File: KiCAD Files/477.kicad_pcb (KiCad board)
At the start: 2 copper layers, 101.7 x 59.5 mm, 74 parts, among them IC1 W25N01GVSFIG, IC2 W25N01GVSFIG, IC3 W25N01GVSFIG, IC4 W25N01GVSFIG, IC5 AZ1117IH-3.3TRG1, IC6 USBLC6-2SC6, J1 BM06B-SRSS-TBT_LF__SN_, J2 6364372-2, J3 TSW-103-14-S-D, J4 TSW-103-14-S-D, J5 BM07B-SRSS-TB_LF__SN_, J6 BM09B-SRSS-TB_LF__SN_, J7 TSW-105-05-F-S, U1 STM32H7A3RGTx, Y1 ABM8G-48.000MHZ-18-D2Y-T

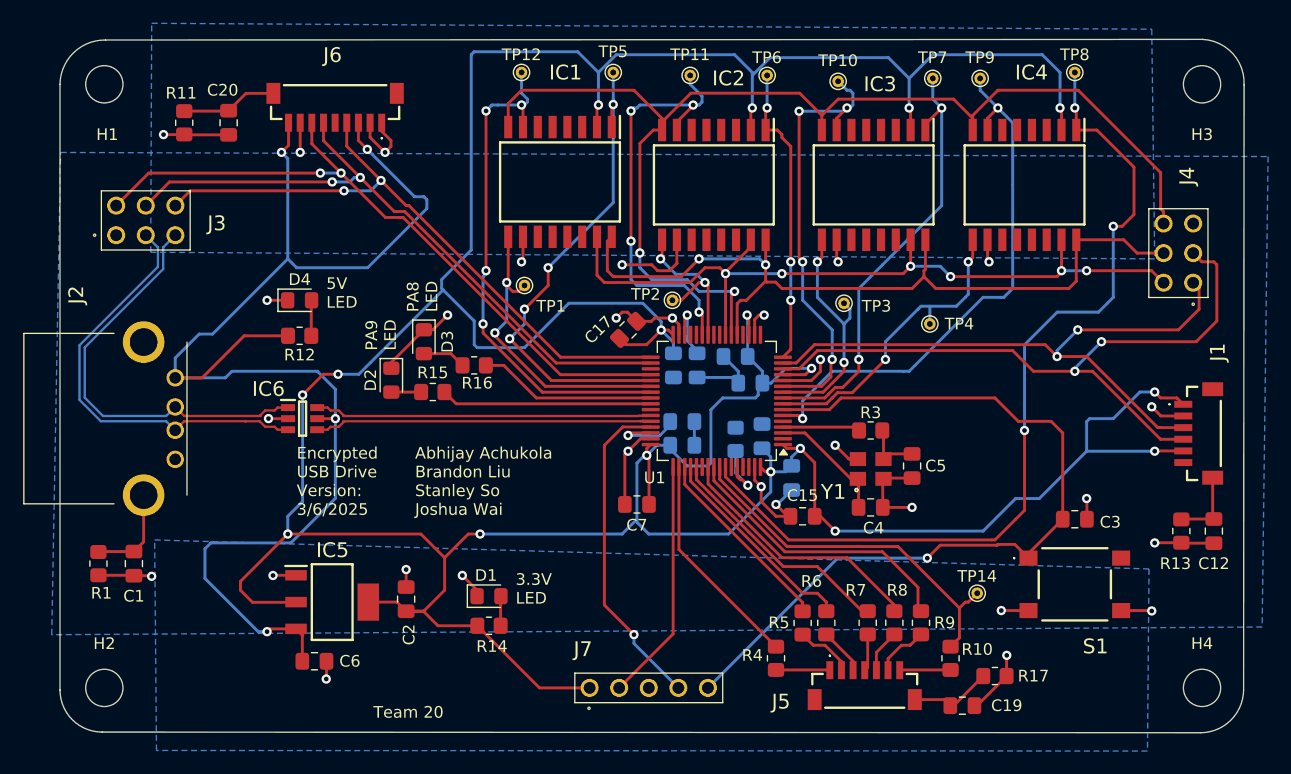
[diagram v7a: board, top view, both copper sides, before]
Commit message: rectangularized the pcb design.
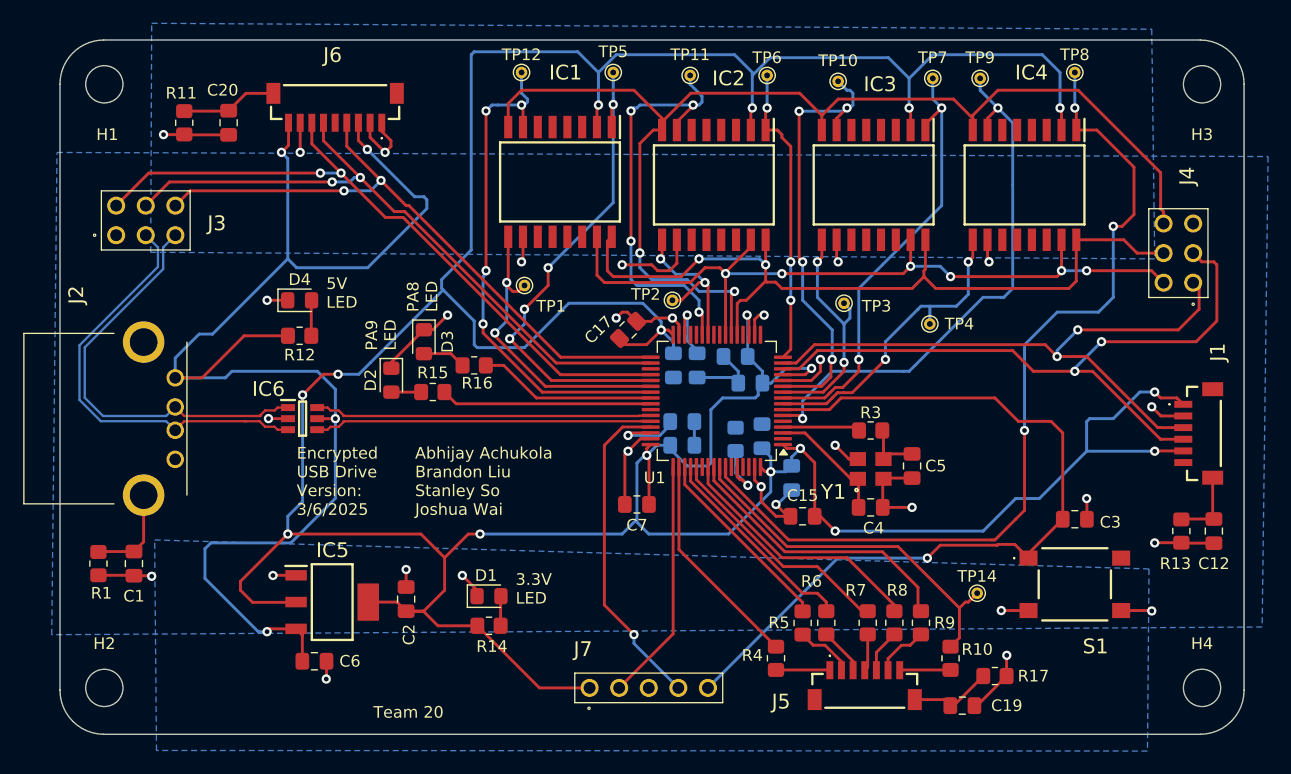
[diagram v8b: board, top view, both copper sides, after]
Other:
- board size 101.7 x 59.5 mm -> 101.7 x 59.6 mm
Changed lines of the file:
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@@
 	)
 	(gr_arc
-		(start 89.22269 135.11063)
-		(mid 86.663558 134.055599)
+		(start 89.35 135.3)
+		(mid 86.687995 134.176649)
 		(end 85.6 131.5)
 		(stroke
@@
 	)
 	(gr_arc
-		(start 187.21063 131.44731)
-		(mid 186.12631 134.077152)
-		(end 183.5 135.17)
+		(start 187.25 131.5)
+		(mid 186.162003 134.176648)
+		(end 183.5 135.3)
 		(stroke
 			(width 0.1)
@@
 	)
 	(gr_line
-		(start 183.69731 75.64669)
-		(end 89.51063 75.7)
+		(start 183.5 75.7)
+		(end 89.35 75.7)
 		(stroke
 			(width 0.1)
@@
 	)
 	(gr_line
-		(start 187.21063 131.44731)
-		(end 187.25 79.55732)
+		(start 187.25 131.5)
+		(end 187.25 79.5)
 		(stroke
 			(width 0.1)
@@
 	)
 	(gr_line
-		(start 89.22269 135.11063)
-		(end 183.5 135.17)
+		(start 89.35 135.3)
+		(end 183.5 135.3)
 		(stroke
 			(width 0.1)
@@
 	)
 	(gr_arc
-		(start 183.69731 75.64669)
-		(mid 186.283573 76.866219)
-		(end 187.25 79.55732)
+		(start 183.5 75.7)
+		(mid 186.161992 76.823363)
+		(end 187.25 79.5)
 		(stroke
 			(width 0.1)
@@
 	(gr_arc
 		(start 85.6 79.5)
-		(mid 86.768308 76.790081)
-		(end 89.51063 75.7)
+		(mid 86.687989 76.823344)
+		(end 89.35 75.7)
 		(stroke
 			(width 0.1)
@@
 		(polygon
 			(pts
-				(xy 85.654 85.352) (xy 189.31 85.704) (xy 188.802 126.09) (xy 84.892 126.754)
+				(xy 85.344 85.352) (xy 189.31 85.704) (xy 188.802 126.09) (xy 84.892 126.754)
 			)
 		)
